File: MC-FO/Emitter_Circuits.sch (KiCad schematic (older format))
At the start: 8 parts, among them U7 74ACT08SCX, U8 IFE98

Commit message: a few more FO tweaks 10-26
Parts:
- C13, C14, C15, C16: footprint (none) -> Capacitor_SMD:C_0603_1608Metric
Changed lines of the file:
@@
 F 0 "C16" V 6900 4800 50  0000 L CNN
 F 1 "100 pF" V 6800 4650 50  0000 L CNN
-F 2 "" H 6700 4800 50  0001 C CNN
+F 2 "Capacitor_SMD:C_0603_1608Metric" H 6700 4800 50  0001 C CNN
 F 3 "~" H 6700 4800 50  0001 C CNN
 	1    6700 4800
@@
 F 0 "C13" H 4950 3250 50  0000 L CNN
 F 1 "0.1 uF" H 4950 3150 50  0000 L CNN
-F 2 "" H 4900 3350 50  0001 C CNN
+F 2 "Capacitor_SMD:C_0603_1608Metric" H 4900 3350 50  0001 C CNN
 F 3 "~" H 4900 3350 50  0001 C CNN
 	1    4900 3350
@@
 F 0 "C15" H 6200 3050 50  0000 L CNN
 F 1 "0.1 uF" H 6200 2950 50  0000 L CNN
-F 2 "" H 6150 3150 50  0001 C CNN
+F 2 "Capacitor_SMD:C_0603_1608Metric" H 6150 3150 50  0001 C CNN
 F 3 "~" H 6150 3150 50  0001 C CNN
 	1    6150 3150
@@
 F 0 "C14" H 5800 3050 50  0000 L CNN
 F 1 "10 uF" H 5800 2950 50  0000 L CNN
-F 2 "" H 5750 3150 50  0001 C CNN
+F 2 "Capacitor_SMD:C_0603_1608Metric" H 5750 3150 50  0001 C CNN
 F 3 "~" H 5750 3150 50  0001 C CNN
 	1    5750 3150

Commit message: added footprints and reference
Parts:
- R7, R8: footprint (none) -> Resistor_SMD:R_0603_1608Metric
- U7: footprint (none) -> Package_SO:SOIC-14_3.9x8.7mm_P1.27mm
- U8: footprint (none) -> Footprints_MC-FO:IFE98
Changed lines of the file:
@@
 $Descr A4 11693 8268
 encoding utf-8
-Sheet 5 11
+Sheet 7 11
 Title ""
 Date ""
@@
 AR Path="/6176CA81/617428A7" Ref="R3"  Part="1"
 AR Path="/6176CAE4/617428A7" Ref="R5"  Part="1"
-F 0 "R7" V 6900 4450 50  0000 L CNN
+F 0 "R11" V 6900 4450 50  0000 L CNN
 F 1 "150 Ohm" V 6800 4200 50  0000 L CNN
-F 2 "" H 6700 4450 50  0001 C CNN
+F 2 "Resistor_SMD:R_0603_1608Metric" H 6700 4450 50  0001 C CNN
 F 3 "~" H 6700 4450 50  0001 C CNN
 	1    6700 4450
@@
 AR Path="/6176CA81/61748E58" Ref="C8"  Part="1"
 AR Path="/6176CAE4/61748E58" Ref="C12"  Part="1"
-F 0 "C16" V 6900 4800 50  0000 L CNN
+F 0 "C24" V 6900 4800 50  0000 L CNN
 F 1 "100 pF" V 6800 4650 50  0000 L CNN
 F 2 "Capacitor_SMD:C_0603_1608Metric" H 6700 4800 50  0001 C CNN
@@
 AR Path="/6176CA81/6178E7F7" Ref="R4"  Part="1"
 AR Path="/6176CAE4/6178E7F7" Ref="R6"  Part="1"
-F 0 "R8" H 7400 3250 50  0000 L CNN
+F 0 "R12" H 7400 3250 50  0000 L CNN
 F 1 "365 Ohm" H 7400 3350 50  0000 L CNN
-F 2 "" H 7300 3300 50  0001 C CNN
+F 2 "Resistor_SMD:R_0603_1608Metric" H 7300 3300 50  0001 C CNN
 F 3 "~" H 7300 3300 50  0001 C CNN
 	1    7300 3300
@@
 AR Path="/6176CA81/6171F0C9" Ref="C5"  Part="1"
 AR Path="/6176CAE4/6171F0C9" Ref="C9"  Part="1"
-F 0 "C13" H 4950 3250 50  0000 L CNN
+F 0 "C21" H 4950 3250 50  0000 L CNN
 F 1 "0.1 uF" H 4950 3150 50  0000 L CNN
 F 2 "Capacitor_SMD:C_0603_1608Metric" H 4900 3350 50  0001 C CNN
@@
 	5950 3500 5750 3500
 $Comp
-L power:GND #PWR04
+L power:GND #PWR07
 U 1 1 61735A2B
 P 5950 3500
-AR Path="/61717EAF/61735A2B" Ref="#PWR04"  Part="1"
-AR Path="/617509F7/61735A2B" Ref="#PWR05"  Part="1"
-AR Path="/61750A2A/61735A2B" Ref="#PWR06"  Part="1"
-AR Path="/6176CA10/61735A2B" Ref="#PWR01"  Part="1"
-AR Path="/6176CA81/61735A2B" Ref="#PWR02"  Part="1"
-AR Path="/6176CAE4/61735A2B" Ref="#PWR03"  Part="1"
-F 0 "#PWR04" H 5950 3250 50  0001 C CNN
+AR Path="/61717EAF/61735A2B" Ref="#PWR07"  Part="1"
+AR Path="/617509F7/61735A2B" Ref="#PWR08"  Part="1"
+AR Path="/61750A2A/61735A2B" Ref="#PWR09"  Part="1"
+AR Path="/6176CA10/61735A2B" Ref="#PWR04"  Part="1"
+AR Path="/6176CA81/61735A2B" Ref="#PWR05"  Part="1"
+AR Path="/6176CAE4/61735A2B" Ref="#PWR06"  Part="1"
+F 0 "#PWR09" H 5950 3250 50  0001 C CNN
 F 1 "GND" H 5955 3327 50  0000 C CNN
 F 2 "" H 5950 3500 50  0001 C CNN
@@
 AR Path="/6176CA81/61733718" Ref="C7"  Part="1"
 AR Path="/6176CAE4/61733718" Ref="C11"  Part="1"
-F 0 "C15" H 6200 3050 50  0000 L CNN
+F 0 "C23" H 6200 3050 50  0000 L CNN
 F 1 "0.1 uF" H 6200 2950 50  0000 L CNN
 F 2 "Capacitor_SMD:C_0603_1608Metric" H 6150 3150 50  0001 C CNN
@@
 AR Path="/6176CA81/61730A88" Ref="C6"  Part="1"
 AR Path="/6176CAE4/61730A88" Ref="C10"  Part="1"
-F 0 "C14" H 5800 3050 50  0000 L CNN
+F 0 "C22" H 5800 3050 50  0000 L CNN
 F 1 "10 uF" H 5800 2950 50  0000 L CNN
 F 2 "Capacitor_SMD:C_0603_1608Metric" H 5750 3150 50  0001 C CNN
@@
 AR Path="/6176CA81/61804FDE" Ref="U3"  Part="1"
 AR Path="/6176CAE4/61804FDE" Ref="U5"  Part="1"
-F 0 "U7" H 4650 4115 50  0000 C CNN
+F 0 "U11" H 4650 4115 50  0000 C CNN
 F 1 "74ACT08SCX" H 4650 4024 50  0000 C CNN
-F 2 "" H 4650 4000 50  0001 C CNN
+F 2 "Package_SO:SOIC-14_3.9x8.7mm_P1.27mm" H 4650 4000 50  0001 C CNN
 F 3 "" H 4650 4000 50  0001 C CNN
 	1    4650 4000
@@
 AR Path="/6176CAE4/61778B54" Ref="U6"  Part="1"
 AR Path="/617509F7/61778B54" Ref="U10"  Part="1"
-F 0 "U8" H 8000 4265 50  0000 C CNN
+F 0 "U12" H 8000 4265 50  0000 C CNN
 F 1 "IFE98" H 8000 4174 50  0000 C CNN
-F 2 "" H 8000 4150 50  0001 C CNN
+F 2 "Footprints_MC-FO:IFE98" H 8000 4150 50  0001 C CNN
 F 3 "" H 8000 4150 50  0001 C CNN
 	1    8000 4150

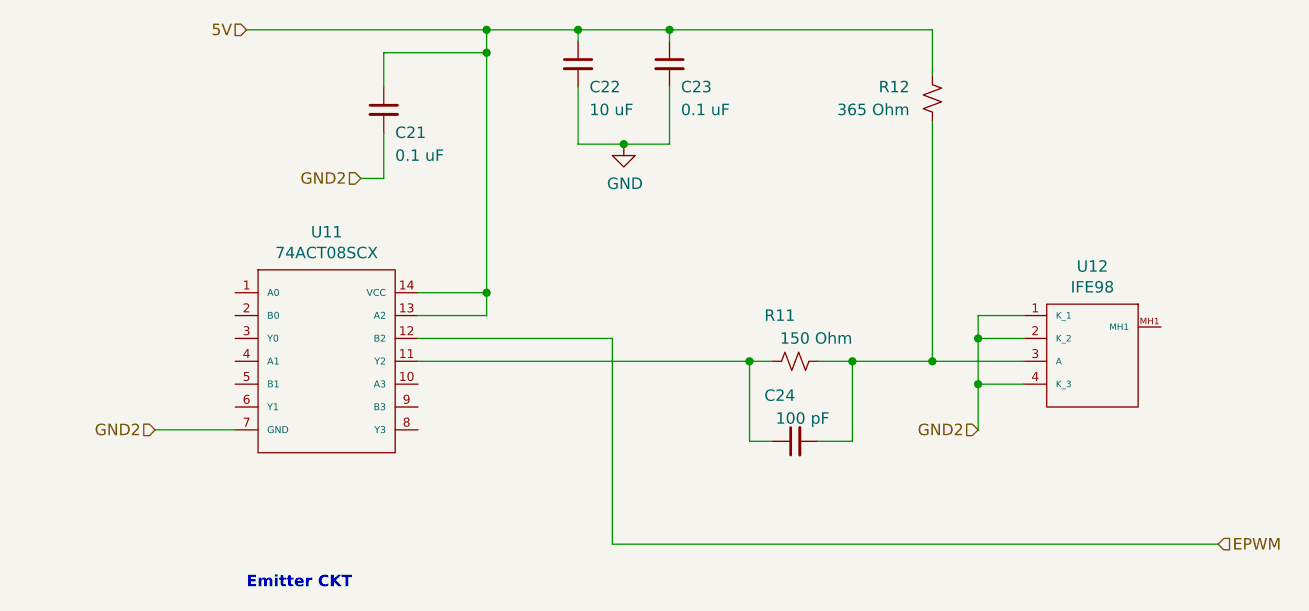
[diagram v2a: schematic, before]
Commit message: floating pins fix, signal name updates
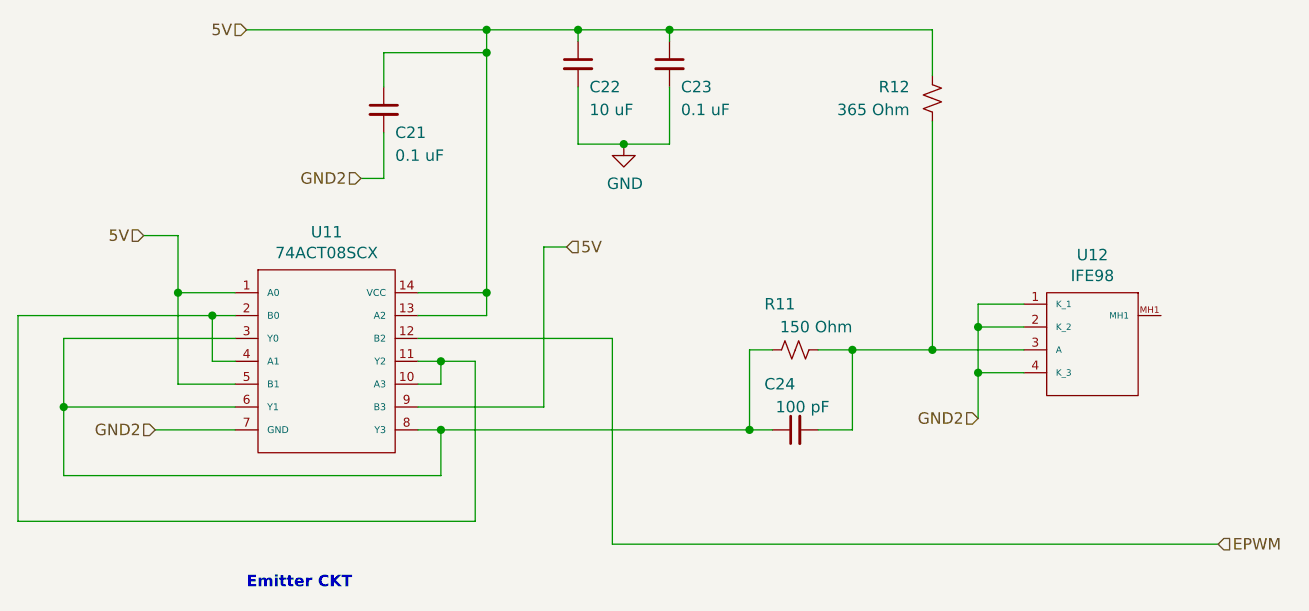
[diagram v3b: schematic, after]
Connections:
- net 5V: now also U7.1 (A0), U7.5 (B1), U7.9 (B3)
- net at C16.1, R7.1: now also U7.3 (Y0), U7.6 (Y1), U7.8 (Y3); no longer U7.11 (Y2)
- net at U7.10 (A3): now also U7.11 (Y2), U7.2 (B0), U7.4 (A1)
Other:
- moved on the sheet: C24, R11, U12
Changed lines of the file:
@@
 L Device:R_Small_US R7
 U 1 1 617428A7
-P 6700 4450
+P 6700 4400
 AR Path="/61717EAF/617428A7" Ref="R7"  Part="1"
 AR Path="/617509F7/617428A7" Ref="R9"  Part="1"
@@
 AR Path="/6176CA81/617428A7" Ref="R3"  Part="1"
 AR Path="/6176CAE4/617428A7" Ref="R5"  Part="1"
-F 0 "R11" V 6900 4450 50  0000 L CNN
-F 1 "150 Ohm" V 6800 4200 50  0000 L CNN
-F 2 "Resistor_SMD:R_0603_1608Metric" H 6700 4450 50  0001 C CNN
-F 3 "~" H 6700 4450 50  0001 C CNN
-	1    6700 4450
+F 0 "R11" V 6900 4400 50  0000 L CNN
+F 1 "150 Ohm" V 6800 4150 50  0000 L CNN
+F 2 "Resistor_SMD:R_0603_1608Metric" H 6700 4400 50  0001 C CNN
+F 3 "~" H 6700 4400 50  0001 C CNN
+	1    6700 4400
 	0    -1   -1   0
 $EndComp
@@
 L Device:C_Small C16
 U 1 1 61748E58
-P 6700 4800
+P 6700 4750
 AR Path="/61717EAF/61748E58" Ref="C16"  Part="1"
 AR Path="/617509F7/61748E58" Ref="C20"  Part="1"
@@
 AR Path="/6176CA81/61748E58" Ref="C8"  Part="1"
 AR Path="/6176CAE4/61748E58" Ref="C12"  Part="1"
-F 0 "C24" V 6900 4800 50  0000 L CNN
-F 1 "100 pF" V 6800 4650 50  0000 L CNN
-F 2 "Capacitor_SMD:C_0603_1608Metric" H 6700 4800 50  0001 C CNN
-F 3 "~" H 6700 4800 50  0001 C CNN
-	1    6700 4800
+F 0 "C24" V 6900 4750 50  0000 L CNN
+F 1 "100 pF" V 6800 4600 50  0000 L CNN
+F 2 "Capacitor_SMD:C_0603_1608Metric" H 6700 4750 50  0001 C CNN
+F 3 "~" H 6700 4750 50  0001 C CNN
+	1    6700 4750
 	0    -1   -1   0
 $EndComp
 Wire Wire Line
-	6500 4450 6500 4800
-Wire Wire Line
-	6500 4800 6600 4800
-Connection ~ 6500 4450
-Wire Wire Line
-	6500 4450 6600 4450
-Wire Wire Line
-	6800 4800 6950 4800
-Wire Wire Line
-	6950 4800 6950 4450
-Wire Wire Line
-	6950 4450 6800 4450
+	6500 4400 6500 4750
+Wire Wire Line
+	6500 4750 6600 4750
+Wire Wire Line
+	6500 4400 6600 4400
+Wire Wire Line
+	6800 4750 6950 4750
+Wire Wire Line
+	6950 4750 6950 4400
+Wire Wire Line
+	6950 4400 6800 4400
 $Comp
 L Device:R_Small_US R8
@@
 	7300 3000 7300 3200
 Wire Wire Line
-	7300 3400 7300 4450
-Wire Wire Line
-	7300 4450 6950 4450
-Connection ~ 6950 4450
-Wire Wire Line
-	7500 4750 7500 4550
-Wire Wire Line
-	7500 4550 7700 4550
-Wire Wire Line
-	7500 4550 7500 4350
-Wire Wire Line
-	7500 4350 7700 4350
-Connection ~ 7500 4550
-Wire Wire Line
-	7500 4350 7500 4250
-Wire Wire Line
-	7500 4250 7700 4250
-Connection ~ 7500 4350
-Connection ~ 7300 4450
-Wire Wire Line
-	7300 4450 7700 4450
+	7300 3400 7300 4400
+Wire Wire Line
+	7300 4400 6950 4400
+Connection ~ 6950 4400
+Wire Wire Line
+	7500 4700 7500 4500
+Wire Wire Line
+	7500 4500 7700 4500
+Wire Wire Line
+	7500 4500 7500 4300
+Wire Wire Line
+	7500 4300 7700 4300
+Connection ~ 7500 4500
+Wire Wire Line
+	7500 4300 7500 4200
+Wire Wire Line
+	7500 4200 7700 4200
+Connection ~ 7500 4300
+Wire Wire Line
+	7300 4400 7700 4400
 Wire Wire Line
 	4900 3100 4900 3250
@@
 Text HLabel 4300 3000 0    50   Input ~ 0
 5V
-Text HLabel 7500 4750 0    50   Input ~ 0
+Text HLabel 7500 4700 0    50   Input ~ 0
 GND2
 Text HLabel 4800 3650 0    50   Input ~ 0
@@
 GND2
 Wire Wire Line
-	5050 4450 6500 4450
-Wire Wire Line
 	5350 3100 5350 4150
 Wire Wire Line
@@
 L Existing_IC_Models:IFE98 U8
 U 1 1 61778B54
-P 8000 4150
+P 8000 4100
 AR Path="/61717EAF/61778B54" Ref="U8"  Part="1"
 AR Path="/61750A2A/61778B54" Ref="U12"  Part="1"
@@
 AR Path="/6176CAE4/61778B54" Ref="U6"  Part="1"
 AR Path="/617509F7/61778B54" Ref="U10"  Part="1"
-F 0 "U12" H 8000 4265 50  0000 C CNN
-F 1 "IFE98" H 8000 4174 50  0000 C CNN
-F 2 "Footprints_MC-FO:IFE98" H 8000 4150 50  0001 C CNN
-F 3 "" H 8000 4150 50  0001 C CNN
-	1    8000 4150
-	1    0    0    -1
-$EndComp
+F 0 "U12" H 8000 4215 50  0000 C CNN
+F 1 "IFE98" H 8000 4124 50  0000 C CNN
+F 2 "Footprints_MC-FO:IFE98" H 8000 4100 50  0001 C CNN
+F 3 "" H 8000 4100 50  0001 C CNN
+	1    8000 4100
+	1    0    0    -1
+$EndComp
+Wire Wire Line
+	5050 4750 5150 4750
+Wire Wire Line
+	3500 4950 5150 4950
+Wire Wire Line
+	5150 4950 5150 4750
+Connection ~ 5150 4750
+Connection ~ 7300 4400
+Wire Wire Line
+	5150 4750 6500 4750
+Connection ~ 6500 4750
+Wire Wire Line
+	5050 4450 5150 4450
+Wire Wire Line
+	5300 4450 5300 5150
+Wire Wire Line
+	5300 5150 3300 5150
+Wire Wire Line
+	3300 5150 3300 4250
+Wire Wire Line
+	3300 4250 4150 4250
+Wire Wire Line
+	3500 4350 4250 4350
+Wire Wire Line
+	3500 4350 3500 4650
+Wire Wire Line
+	3500 4650 4250 4650
+Connection ~ 3500 4650
+Wire Wire Line
+	3500 4650 3500 4950
+Wire Wire Line
+	4150 4250 4150 4450
+Wire Wire Line
+	4150 4450 4250 4450
+Connection ~ 4150 4250
+Wire Wire Line
+	4150 4250 4250 4250
+Wire Wire Line
+	5150 4450 5150 4550
+Wire Wire Line
+	5150 4550 5050 4550
+Connection ~ 5150 4450
+Wire Wire Line
+	5150 4450 5300 4450
+Text HLabel 3850 3900 0    50   Input ~ 0
+5V
+Text HLabel 5700 3950 2    50   Input ~ 0
+5V
+Wire Wire Line
+	5700 3950 5600 3950
+Wire Wire Line
+	5600 3950 5600 4650
+Wire Wire Line
+	5600 4650 5050 4650
+Wire Wire Line
+	3850 3900 4000 3900
+Wire Wire Line
+	4000 3900 4000 4150
+Wire Wire Line
+	4000 4550 4250 4550
+Wire Wire Line
+	4000 4150 4250 4150
+Connection ~ 4000 4150
+Wire Wire Line
+	4000 4150 4000 4550
 $EndSCHEMATC

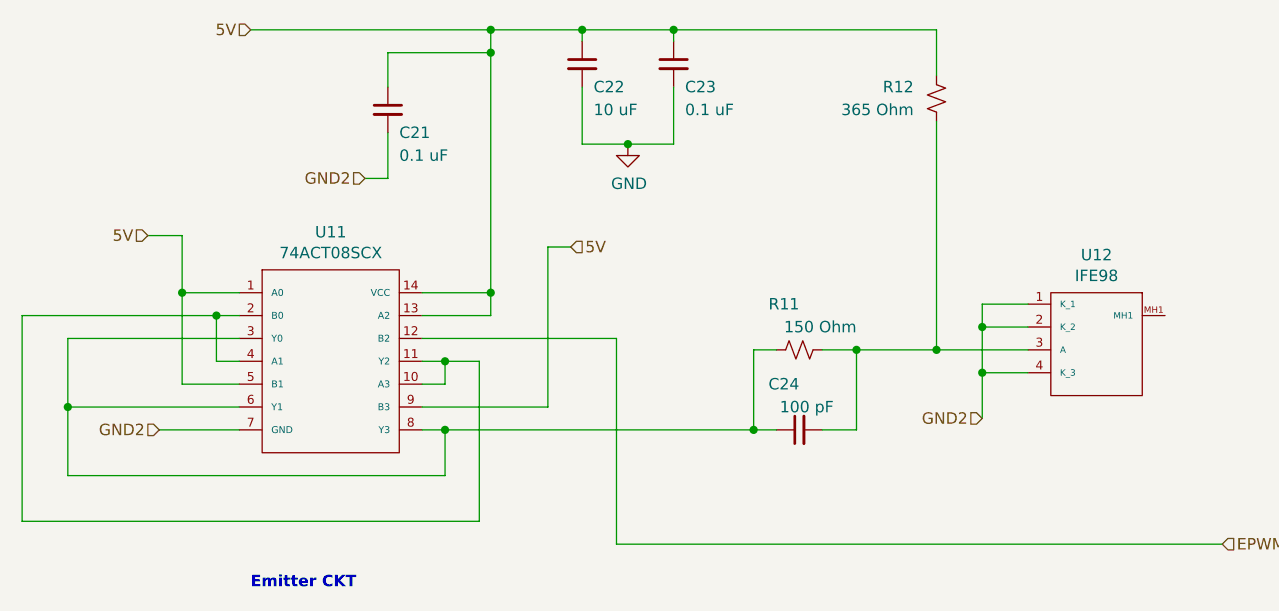
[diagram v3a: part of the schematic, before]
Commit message: C31-34 larger packaging and part assignment
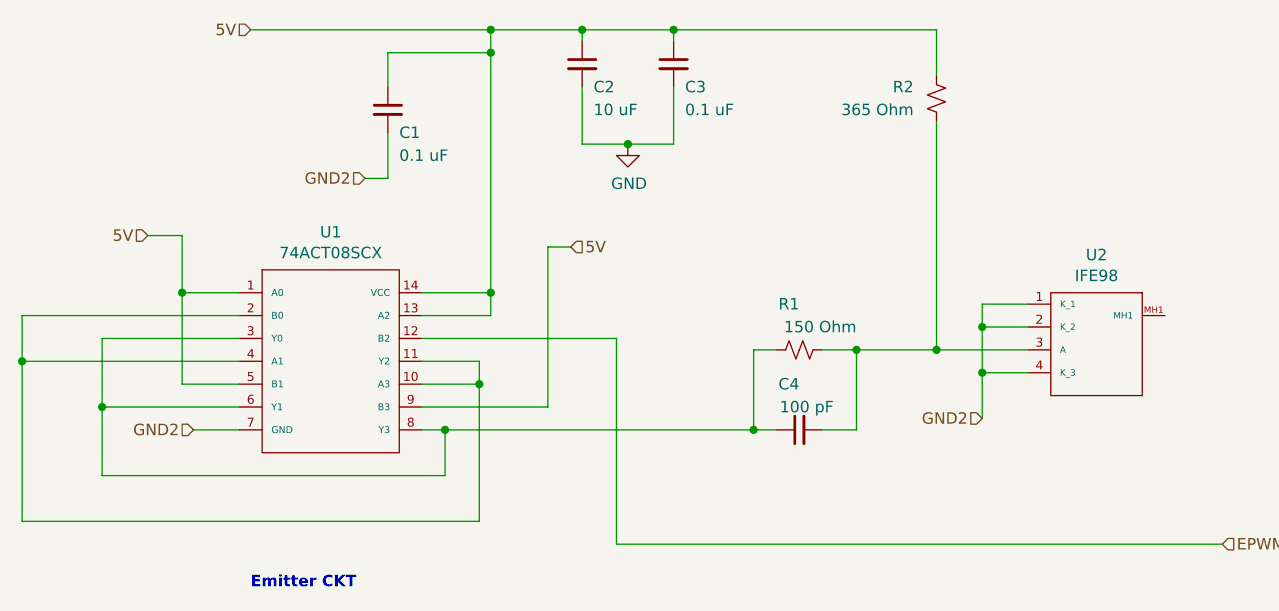
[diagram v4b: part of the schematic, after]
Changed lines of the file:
@@
 $Descr A4 11693 8268
 encoding utf-8
-Sheet 7 11
+Sheet 2 11
 Title ""
 Date ""
@@
 AR Path="/6176CA81/617428A7" Ref="R3"  Part="1"
 AR Path="/6176CAE4/617428A7" Ref="R5"  Part="1"
-F 0 "R11" V 6900 4400 50  0000 L CNN
+F 0 "R1" V 6900 4400 50  0000 L CNN
 F 1 "150 Ohm" V 6800 4150 50  0000 L CNN
 F 2 "Resistor_SMD:R_0603_1608Metric" H 6700 4400 50  0001 C CNN
@@
 AR Path="/6176CA81/61748E58" Ref="C8"  Part="1"
 AR Path="/6176CAE4/61748E58" Ref="C12"  Part="1"
-F 0 "C24" V 6900 4750 50  0000 L CNN
+F 0 "C4" V 6900 4750 50  0000 L CNN
 F 1 "100 pF" V 6800 4600 50  0000 L CNN
 F 2 "Capacitor_SMD:C_0603_1608Metric" H 6700 4750 50  0001 C CNN
@@
 AR Path="/6176CA81/6178E7F7" Ref="R4"  Part="1"
 AR Path="/6176CAE4/6178E7F7" Ref="R6"  Part="1"
-F 0 "R12" H 7400 3250 50  0000 L CNN
+F 0 "R2" H 7400 3250 50  0000 L CNN
 F 1 "365 Ohm" H 7400 3350 50  0000 L CNN
 F 2 "Resistor_SMD:R_0603_1608Metric" H 7300 3300 50  0001 C CNN
@@
 AR Path="/6176CA81/6171F0C9" Ref="C5"  Part="1"
 AR Path="/6176CAE4/6171F0C9" Ref="C9"  Part="1"
-F 0 "C21" H 4950 3250 50  0000 L CNN
+F 0 "C1" H 4950 3250 50  0000 L CNN
 F 1 "0.1 uF" H 4950 3150 50  0000 L CNN
 F 2 "Capacitor_SMD:C_0603_1608Metric" H 4900 3350 50  0001 C CNN
@@
 AR Path="/6176CA81/61735A2B" Ref="#PWR05"  Part="1"
 AR Path="/6176CAE4/61735A2B" Ref="#PWR06"  Part="1"
-F 0 "#PWR09" H 5950 3250 50  0001 C CNN
+F 0 "#PWR04" H 5950 3250 50  0001 C CNN
 F 1 "GND" H 5955 3327 50  0000 C CNN
 F 2 "" H 5950 3500 50  0001 C CNN
@@
 AR Path="/6176CA81/61733718" Ref="C7"  Part="1"
 AR Path="/6176CAE4/61733718" Ref="C11"  Part="1"
-F 0 "C23" H 6200 3050 50  0000 L CNN
+F 0 "C3" H 6200 3050 50  0000 L CNN
 F 1 "0.1 uF" H 6200 2950 50  0000 L CNN
 F 2 "Capacitor_SMD:C_0603_1608Metric" H 6150 3150 50  0001 C CNN
@@
 AR Path="/6176CA81/61730A88" Ref="C6"  Part="1"
 AR Path="/6176CAE4/61730A88" Ref="C10"  Part="1"
-F 0 "C22" H 5800 3050 50  0000 L CNN
+F 0 "C2" H 5800 3050 50  0000 L CNN
 F 1 "10 uF" H 5800 2950 50  0000 L CNN
 F 2 "Capacitor_SMD:C_0603_1608Metric" H 5750 3150 50  0001 C CNN
@@
 Connection ~ 5350 3100
 Wire Wire Line
-	3900 4750 4250 4750
+	4050 4750 4250 4750
 $Comp
 L Existing_IC_Models:74ACT08SCX U7
@@
 AR Path="/6176CA81/61804FDE" Ref="U3"  Part="1"
 AR Path="/6176CAE4/61804FDE" Ref="U5"  Part="1"
-F 0 "U11" H 4650 4115 50  0000 C CNN
+F 0 "U1" H 4650 4115 50  0000 C CNN
 F 1 "74ACT08SCX" H 4650 4024 50  0000 C CNN
 F 2 "Package_SO:SOIC-14_3.9x8.7mm_P1.27mm" H 4650 4000 50  0001 C CNN
@@
 	1    0    0    -1
 $EndComp
-Text HLabel 3900 4750 0    50   Input ~ 0
+Text HLabel 4050 4750 0    50   Input ~ 0
 GND2
 Wire Wire Line
@@
 AR Path="/6176CAE4/61778B54" Ref="U6"  Part="1"
 AR Path="/617509F7/61778B54" Ref="U10"  Part="1"
-F 0 "U12" H 8000 4215 50  0000 C CNN
+F 0 "U2" H 8000 4215 50  0000 C CNN
 F 1 "IFE98" H 8000 4124 50  0000 C CNN
 F 2 "Footprints_MC-FO:IFE98" H 8000 4100 50  0001 C CNN
@@
 	5050 4750 5150 4750
 Wire Wire Line
-	3500 4950 5150 4950
+	3650 4950 5150 4950
 Wire Wire Line
 	5150 4950 5150 4750
@@
 Connection ~ 6500 4750
 Wire Wire Line
-	5050 4450 5150 4450
-Wire Wire Line
-	5300 4450 5300 5150
+	5050 4450 5300 4450
+Wire Wire Line
+	5300 4450 5300 4550
 Wire Wire Line
 	5300 5150 3300 5150
 Wire Wire Line
-	3300 5150 3300 4250
-Wire Wire Line
-	3300 4250 4150 4250
-Wire Wire Line
-	3500 4350 4250 4350
-Wire Wire Line
-	3500 4350 3500 4650
-Wire Wire Line
-	3500 4650 4250 4650
-Connection ~ 3500 4650
-Wire Wire Line
-	3500 4650 3500 4950
-Wire Wire Line
-	4150 4250 4150 4450
-Wire Wire Line
-	4150 4450 4250 4450
-Connection ~ 4150 4250
-Wire Wire Line
-	4150 4250 4250 4250
-Wire Wire Line
-	5150 4450 5150 4550
-Wire Wire Line
-	5150 4550 5050 4550
-Connection ~ 5150 4450
-Wire Wire Line
-	5150 4450 5300 4450
+	3300 5150 3300 4450
+Wire Wire Line
+	3650 4650 4250 4650
+Wire Wire Line
+	3650 4650 3650 4950
+Wire Wire Line
+	3300 4250 4250 4250
 Text HLabel 3850 3900 0    50   Input ~ 0
 5V
@@
 Wire Wire Line
 	4000 4150 4000 4550
+Wire Wire Line
+	3300 4450 4250 4450
+Connection ~ 3300 4450
+Wire Wire Line
+	3300 4450 3300 4250
+Wire Wire Line
+	5050 4550 5300 4550
+Connection ~ 5300 4550
+Wire Wire Line
+	5300 4550 5300 5150
+Wire Wire Line
+	4250 4350 3650 4350
+Wire Wire Line
+	3650 4350 3650 4650
+Connection ~ 3650 4650
 $EndSCHEMATC
